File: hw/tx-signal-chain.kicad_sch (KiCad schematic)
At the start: 9 parts, among them Q401 IRFP250NPBF, U401 UCC27511ADBV

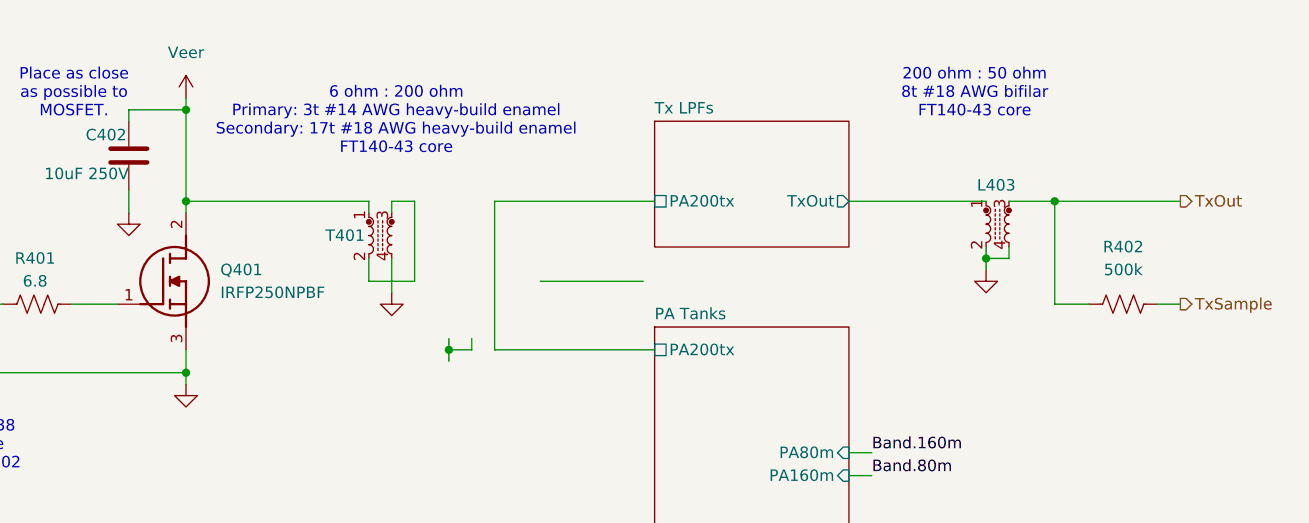
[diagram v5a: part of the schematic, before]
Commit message: Finish up tx 200 ohm -> 50 ohm matching transformer
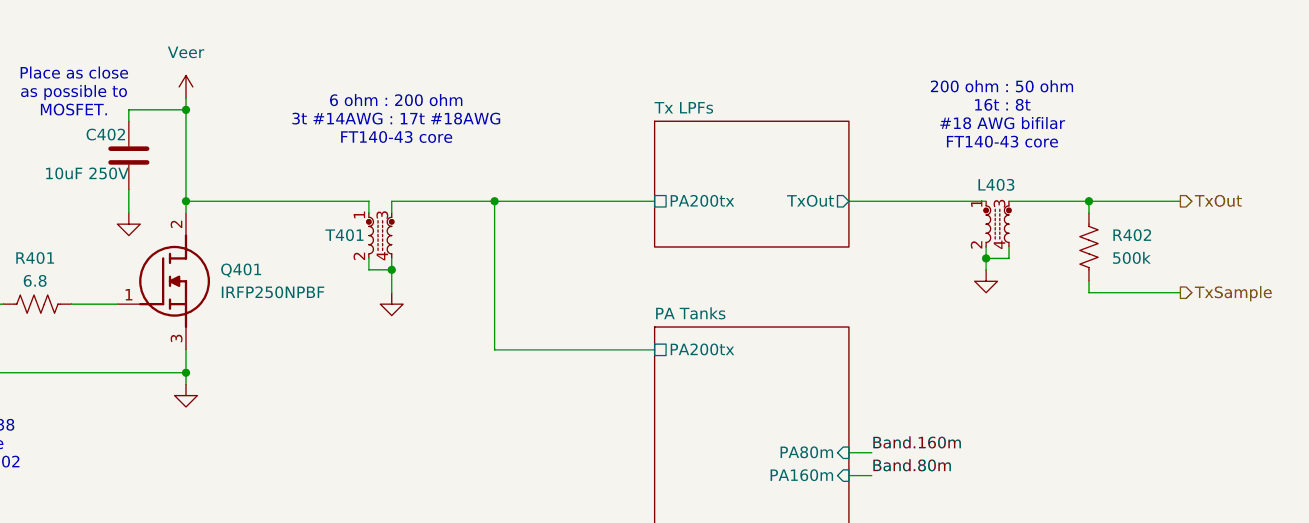
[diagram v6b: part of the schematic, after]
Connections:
- net GND: now also T401.2
- net PA Tanks/PA200tx: now also T401.3
- net TxOut: now also R402.2; no longer R402.1
- net TxSample: now also R402.1; no longer R402.2
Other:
- note added: "200 ohm : 50 ohm 16t : 8t #18 AWG bifilar FT140-43 core"
- note added: "6 ohm : 200 ohm 3t #14AWG : 17t #18AWG FT140-43 core"
- note removed: "200 ohm : 50 ohm 8t #18 AWG bifilar FT140-43 core"
- note removed: "6 ohm : 200 ohm Primary: 3t #14 AWG heavy-build enamel Secondary: 17t #18 AWG heavy-build enamel FT140-43 core"
- moved on the sheet: R402
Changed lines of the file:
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@@
 		(comment 1 "Alan Mimms")
 	)
-	(text "200 ohm : 50 ohm\n8t #18 AWG bifilar\nFT140-43 core"
+	(text "200 ohm : 50 ohm\n16t : 8t\n#18 AWG bifilar\nFT140-43 core"
 		(exclude_from_sim no)
-		(at 231.14 61.722 0)
-		(effects
-			(font
-				(size 1.27 1.27)
-			)
-		)
-	)
-	(text "6 ohm : 200 ohm\nPrimary: 3t #14 AWG heavy-build enamel\nSecondary: 17t #18 AWG heavy-build enamel\nFT140-43 core"
+		(at 234.188 64.262 0)
+		(effects
+			(font
+				(size 1.27 1.27)
+			)
+		)
+	)
+	(text "6 ohm : 200 ohm\n3t #14AWG : 17t #18AWG\nFT140-43 core"
 		(exclude_from_sim no)
 		(at 166.878 64.77 0)
@@
 	)
 	(junction
-		(at 143.51 73.66)
+		(at 166.37 81.28)
 		(diameter 0)
 		(color 0 0 0 0)
 	)
 	(junction
-		(at 172.72 90.17)
+		(at 177.8 73.66)
+		(diameter 0)
+		(color 0 0 0 0)
+	)
+	(junction
+		(at 143.51 73.66)
 		(diameter 0)
 		(color 0 0 0 0)
@@
 	)
 	(junction
+		(at 243.84 73.66)
+		(diameter 0)
+		(color 0 0 0 0)
+	)
+	(junction
 		(at 143.51 92.71)
 		(diameter 0)
 		(color 0 0 0 0)
 	)
-	(junction
-		(at 240.03 73.66)
-		(diameter 0)
-		(color 0 0 0 0)
-	)
 	(wire
 		(pts
@@
 	(wire
 		(pts
-			(xy 251.46 85.09) (xy 254 85.09)
-		)
-		(stroke
-			(width 0)
-			(type default)
-		)
-	)
-	(wire
-		(pts
 			(xy 114.3 85.09) (xy 118.11 85.09)
 		)
@@
 	(wire
 		(pts
-			(xy 166.37 73.66) (xy 168.91 73.66)
+			(xy 166.37 73.66) (xy 177.8 73.66)
 		)
 		(stroke
@@
 	(wire
 		(pts
-			(xy 163.83 80.01) (xy 163.83 82.55)
+			(xy 163.83 81.28) (xy 166.37 81.28)
+		)
+		(stroke
+			(width 0)
+			(type default)
+		)
+	)
+	(wire
+		(pts
+			(xy 163.83 80.01) (xy 163.83 81.28)
 		)
 		(stroke
@@
 	(wire
 		(pts
+			(xy 243.84 73.66) (xy 254 73.66)
+		)
+		(stroke
+			(width 0)
+			(type default)
+		)
+	)
+	(wire
+		(pts
 			(xy 137.16 63.5) (xy 143.51 63.5)
 		)
@@
 	(wire
 		(pts
+			(xy 243.84 83.82) (xy 254 83.82)
+		)
+		(stroke
+			(width 0)
+			(type default)
+		)
+	)
+	(wire
+		(pts
 			(xy 143.51 92.71) (xy 143.51 90.17)
 		)
@@
 	(wire
 		(pts
+			(xy 166.37 81.28) (xy 166.37 83.82)
+		)
+		(stroke
+			(width 0)
+			(type default)
+		)
+	)
+	(wire
+		(pts
 			(xy 232.41 80.01) (xy 232.41 81.28)
 		)
@@
 	(wire
 		(pts
-			(xy 166.37 80.01) (xy 166.37 83.82)
+			(xy 166.37 80.01) (xy 166.37 81.28)
+		)
+		(stroke
+			(width 0)
+			(type default)
+		)
+	)
+	(wire
+		(pts
+			(xy 243.84 82.55) (xy 243.84 83.82)
 		)
 		(stroke
@@
 	(wire
 		(pts
-			(xy 182.88 82.55) (xy 194.31 82.55)
-		)
-		(stroke
-			(width 0)
-			(type default)
-		)
-	)
-	(wire
-		(pts
-			(xy 175.26 90.17) (xy 172.72 90.17)
+			(xy 243.84 73.66) (xy 243.84 74.93)
 		)
 		(stroke
@@
 	(wire
 		(pts
-			(xy 240.03 73.66) (xy 254 73.66)
-		)
-		(stroke
-			(width 0)
-			(type default)
-		)
-	)
-	(wire
-		(pts
-			(xy 163.83 82.55) (xy 168.91 82.55)
-		)
-		(stroke
-			(width 0)
-			(type default)
-		)
-	)
-	(wire
-		(pts
-			(xy 172.72 88.9) (xy 172.72 90.17)
-		)
-		(stroke
-			(width 0)
-			(type default)
-		)
-	)
-	(wire
-		(pts
-			(xy 243.84 85.09) (xy 240.03 85.09)
-		)
-		(stroke
-			(width 0)
-			(type default)
-		)
-	)
-	(wire
-		(pts
 			(xy 92.71 90.17) (xy 93.98 90.17)
 		)
@@
 	(wire
 		(pts
-			(xy 240.03 85.09) (xy 240.03 73.66)
-		)
-		(stroke
-			(width 0)
-			(type default)
-		)
-	)
-	(wire
-		(pts
 			(xy 118.11 92.71) (xy 118.11 91.44)
 		)
@@
 	(wire
 		(pts
-			(xy 172.72 90.17) (xy 172.72 91.44)
-		)
-		(stroke
-			(width 0)
-			(type default)
-		)
-	)
-	(wire
-		(pts
 			(xy 143.51 93.98) (xy 143.51 92.71)
 		)
@@
 	(wire
 		(pts
-			(xy 234.95 73.66) (xy 240.03 73.66)
+			(xy 234.95 73.66) (xy 243.84 73.66)
 		)
 		(stroke
@@
 	(wire
 		(pts
-			(xy 168.91 73.66) (xy 168.91 82.55)
-		)
-		(stroke
-			(width 0)
-			(type default)
-		)
-	)
-	(wire
-		(pts
 			(xy 91.44 85.09) (xy 93.98 85.09)
 		)
@@
 		(pts
 			(xy 143.51 73.66) (xy 163.83 73.66)
-		)
-		(stroke
-			(width 0)
-			(type default)
-		)
-	)
-	(wire
-		(pts
-			(xy 175.26 88.9) (xy 175.26 90.17)
 		)
 		(stroke
@@
 	(hierarchical_label "TxSample"
 		(shape output)
-		(at 254 85.09 0)
+		(at 254 83.82 0)
 		(effects
 			(font
@@
 		(length 2.54)
 		(shape round)
-		(at 223.52 73.66 0)
+		(at 227.33 73.66 0)
 		(effects
 			(font
@@
 		)
 		(property "Netclass" "PowerRF"
-			(at 223.52 70.358 0)
-			(effects
-				(font
-					(size 1.27 1.27)
-				)
-				(justify left)
+			(at 227.33 70.358 0)
+			(effects
+				(font
+					(size 1.27 1.27)
+				)
+				(justify right)
 			)
 		)
 		(property "Component Class" ""
-			(at 184.15 111.76 0)
+			(at 266.7 111.76 0)
 			(effects
 				(font
@@
 					(italic yes)
 				)
-				(justify left)
+				(justify right)
 				(hide yes)
 			)
@@
 				)
 				(justify right)
-				(hide yes)
-			)
-		)
-	)
-	(netclass_flag ""
-		(length 2.54)
-		(shape round)
-		(at 175.26 73.66 0)
-		(effects
-			(font
-				(size 1.27 1.27)
-			)
-			(justify left bottom)
-		)
-		(property "Netclass" "PowerRF"
-			(at 175.26 70.358 0)
-			(effects
-				(font
-					(size 1.27 1.27)
-				)
-				(justify left)
-			)
-		)
-		(property "Component Class" ""
-			(at 135.89 111.76 0)
-			(effects
-				(font
-					(size 1.27 1.27)
-					(italic yes)
-				)
-				(justify left)
 				(hide yes)
 			)
@@
 	(symbol
 		(lib_id "Device:R_US")
-		(at 247.65 85.09 90)
+		(at 243.84 78.74 180)
 		(unit 1)
 		(exclude_from_sim no)
@@
 		(fields_autoplaced yes)
 		(property "Reference" "R402"
-			(at 247.65 78.74 90)
-			(effects
-				(font
-					(size 1.27 1.27)
-				)
+			(at 246.38 77.4699 0)
+			(effects
+				(font
+					(size 1.27 1.27)
+				)
+				(justify right)
 			)
 		)
 		(property "Value" "500k"
-			(at 247.65 81.28 90)
-			(effects
-				(font
-					(size 1.27 1.27)
-				)
+			(at 246.38 80.0099 0)
+			(effects
+				(font
+					(size 1.27 1.27)
+				)
+				(justify right)
 			)
 		)
 		(property "Footprint" "Resistor_SMD:R_0603_1608Metric"
-			(at 247.904 84.074 90)
+			(at 242.824 78.486 90)
 			(effects
 				(font
@@
 		)
 		(property "Datasheet" "~"
-			(at 247.65 85.09 0)
+			(at 243.84 78.74 0)
 			(effects
 				(font
@@
 		)
 		(property "Description" "Resistor, US symbol"
-			(at 247.65 85.09 0)
+			(at 243.84 78.74 0)
 			(effects
 				(font
@@
 		)
 		(property "DigiKey_Part_Number" ""
-			(at 247.65 85.09 90)
+			(at 243.84 78.74 90)
 			(effects
 				(font
@@
 		)
 		(property "Display" ""
-			(at 247.65 85.09 90)
+			(at 243.84 78.74 90)
 			(effects
 				(font
@@
 		)
 		(property "Display 2" ""
-			(at 247.65 85.09 90)
+			(at 243.84 78.74 90)
 			(effects
 				(font
@@
 		)
 		(property "Mfg" ""
-			(at 247.65 85.09 90)
+			(at 243.84 78.74 90)
 			(effects
 				(font
@@
 		)
 		(property "MfgPart" ""
-			(at 247.65 85.09 90)
+			(at 243.84 78.74 90)
 			(effects
 				(font
@@
 		)
 		(property "Sim.Params" ""
-			(at 247.65 85.09 90)
+			(at 243.84 78.74 90)
 			(effects
 				(font
@@
 		)
 		(property "Sim.Type" ""
-			(at 247.65 85.09 90)
-			(effects
-				(font
+			(at 243.84 78.74 90)
+			(effects
+				(font

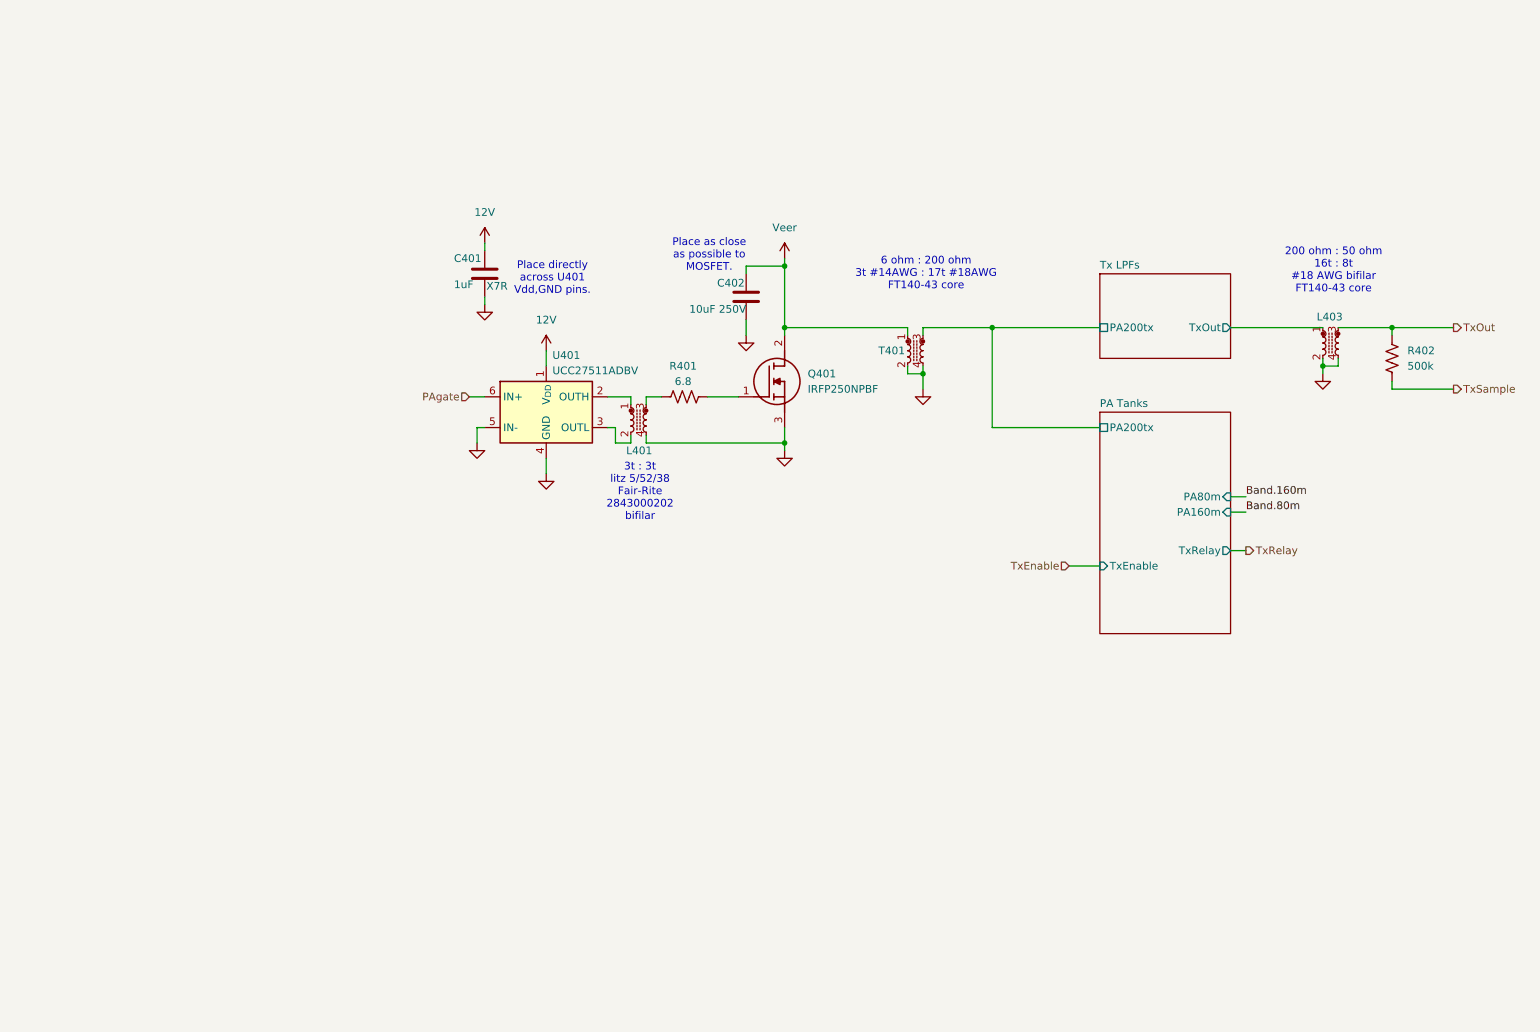
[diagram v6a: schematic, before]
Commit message: Moved ant page into tx page, added Bruene Direction Coupler to measure VSWR. General cleanup, page renumber, reannote
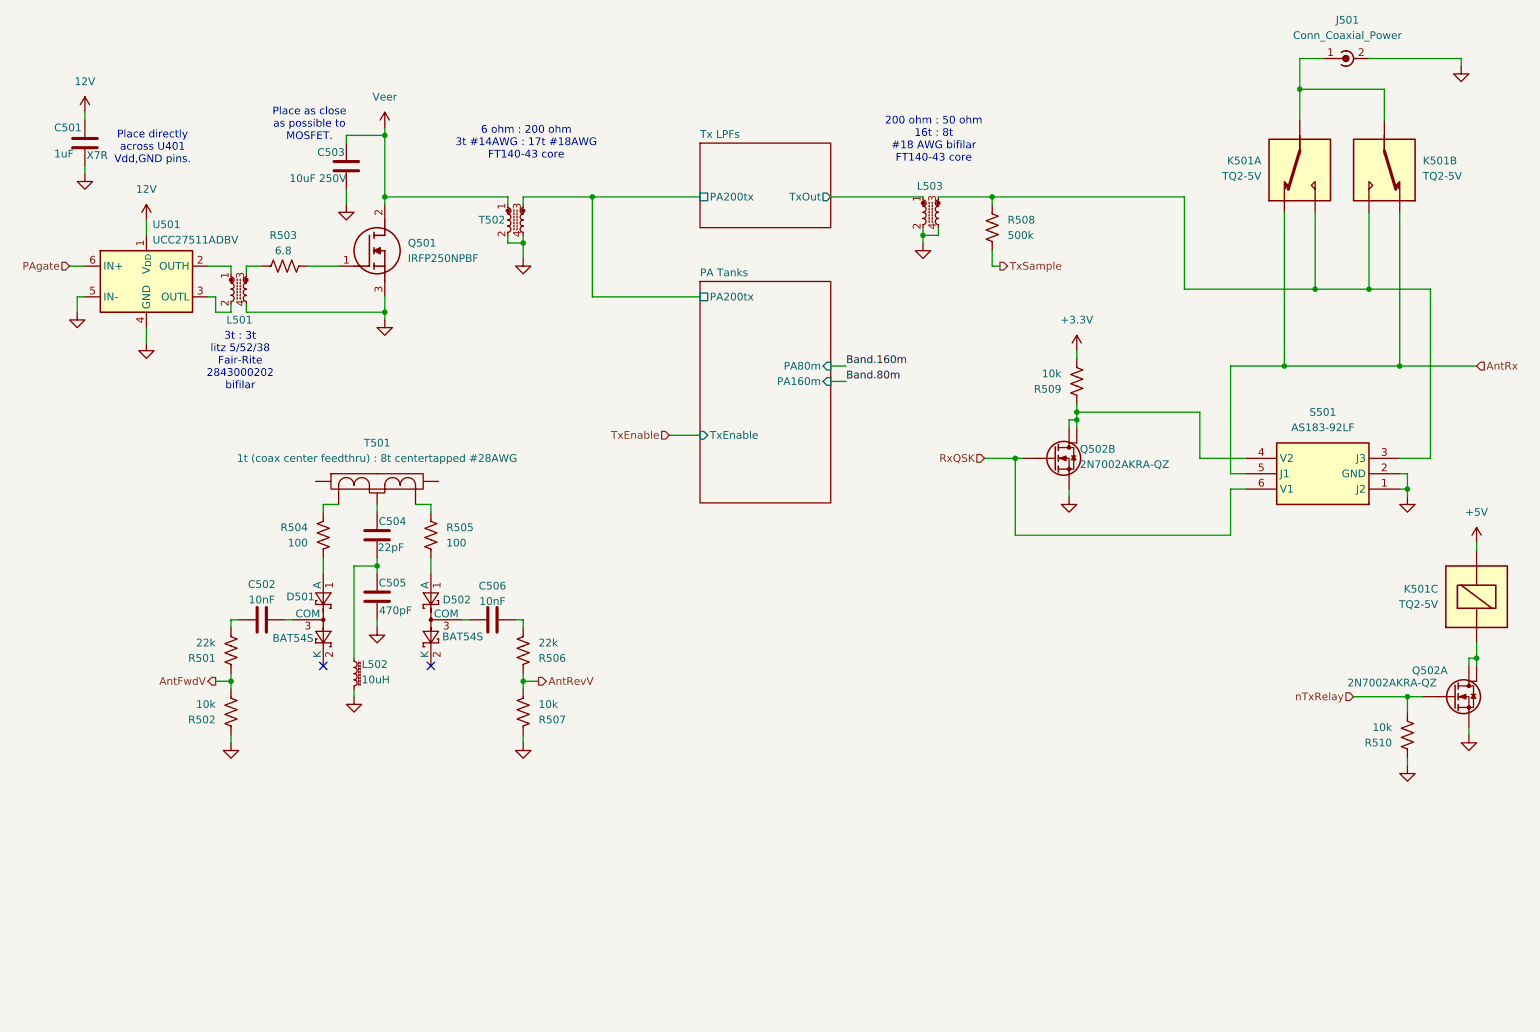
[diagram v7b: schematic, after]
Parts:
- added C502, C506: 10nF, symbol Device:C
- added C504: 22pF, symbol Device:C
- added C505: 470pF, symbol Device:C
- added D501, D502: BAT54S, Package_TO_SOT_SMD:SOT-23, symbol Diode:BAT54S
- added J501: Conn_Coaxial_Power, Connector_Coaxial:SMA_Amphenol_132289_EdgeMount, symbol Connector:Conn_Coaxial_Power
- added K501: TQ2-5V, symbol Library:TQ2-5V
- added L502: 10uH, symbol Device:L_Ferrite_Small
- added Q502: 2N7002AKRA-QZ, 2N7002AKRAQZ, symbol 2N7002AKRA-QZ:2N7002AKRA-QZ
- added R501, R506: 22k, symbol Device:R_US
- added R502, R507, R509, R510: 10k, symbol Device:R_US
- added R504, R505: 100, symbol Device:R_US
- added S501: AS183-92LF, SOT65P220X110-6N, symbol AS183-92LF:AS183-92LF
- added T501: 1t (coax center feedthru) : 8t centertapped #28AWG, symbol Library:Tandem_Coupler
- renumbered C401 to C501, C402 to C503, L401 to L501, L403 to L503, Q401 to Q501, R401 to R503, R402 to R508, T401 to T502, U401 to U501
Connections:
- net GND: now also C505.2, J501.2 (Ext), L502.2, Q502.1 (S1), Q502.4 (S2), R502.1, R507.1, R510.1, S501.1 (J2), S501.2 (GND)
- net TxOut: no longer names the net of L503.3, R508.2
- net TxOut: now also K501.4 (NO1), K501.9, K501.9, S501.3 (J3)
- new net: C504.2, C505.1, L502.1
- new net: D502.1 (A), R505.2
- new net: C506.2, D502.3 (COM)
- new net: R504.1, T501.5
- new net: D501.1 (A), R504.2
- new net: Q502.3 (D2_1), Q502.8 (D2_2), R509.1, S501.4 (V2)
- new net: C504.1, T501.3
- new net: R505.1, T501.4
- new net: C502.2, D501.3 (COM)
- new net: J501.1 (In), K501.16, K501.16, K501.3 (T1), K501.4, K501.4 (NO1), K501.6 (T2)
- new net: C502.1, R501.2
- new net: C506.1, R506.2
- new net: K501.9 (C1), Q502.6 (D1), Q502.7 (D2)
- new net +3.3V: R509.2
- new net +5V: K501.10 (C2)
- new net AntFwdV: R501.1, R502.2
- new net AntRevV: R506.1, R507.2
- new net AntRx: K501.5 (NC1), K501.6, K501.6 (T2), K501.8 (NC2), S501.5 (J1)
- new net RxQSK: Q502.5 (G2), S501.6 (V1)
- new net nTxRelay: Q502.2 (G1), R510.2
- no-connect marks 0 -> 2
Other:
- sheet PA Tanks ports: added none; removed TxRelay
- moved on the sheet: C501, C503, L501, L503, Q501, R503, R508, T502, U501
